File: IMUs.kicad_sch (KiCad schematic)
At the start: 15 parts, among them U501 LSM6DSL, U502 DPS368

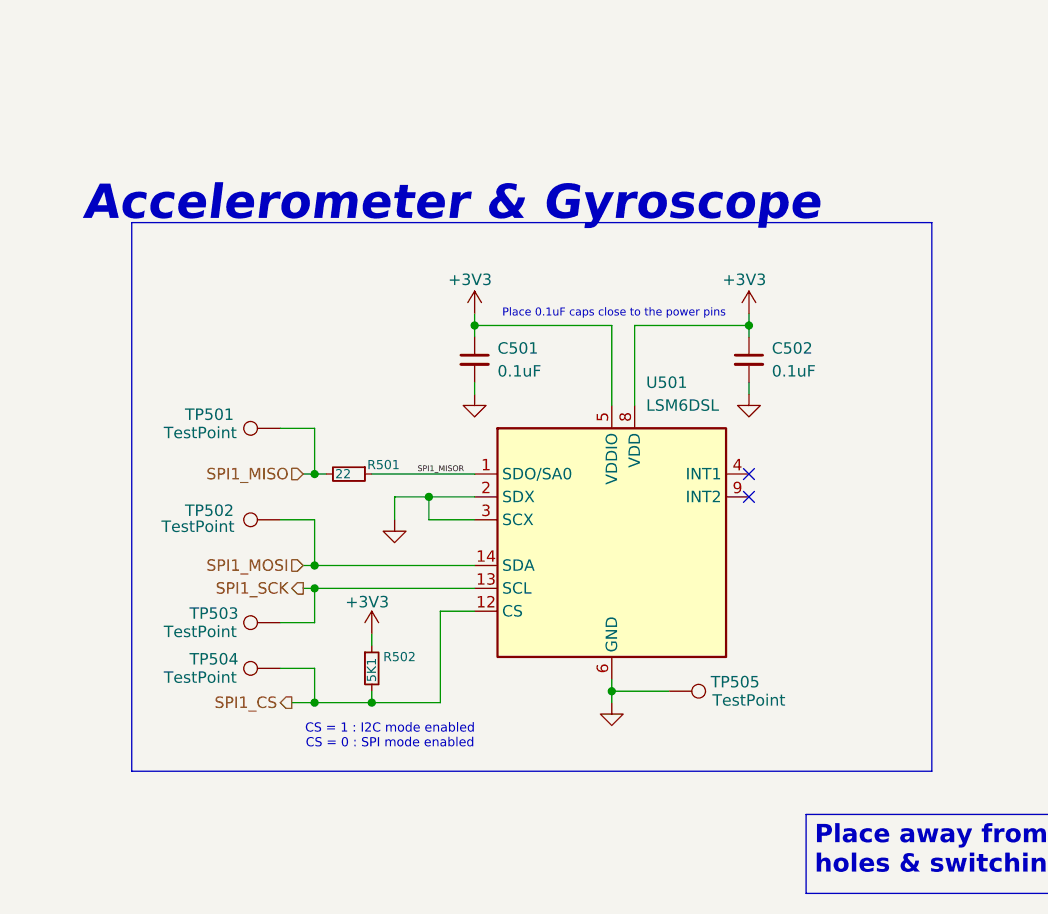
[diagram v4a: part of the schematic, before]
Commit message: refactor: change motor output, renamed power nets
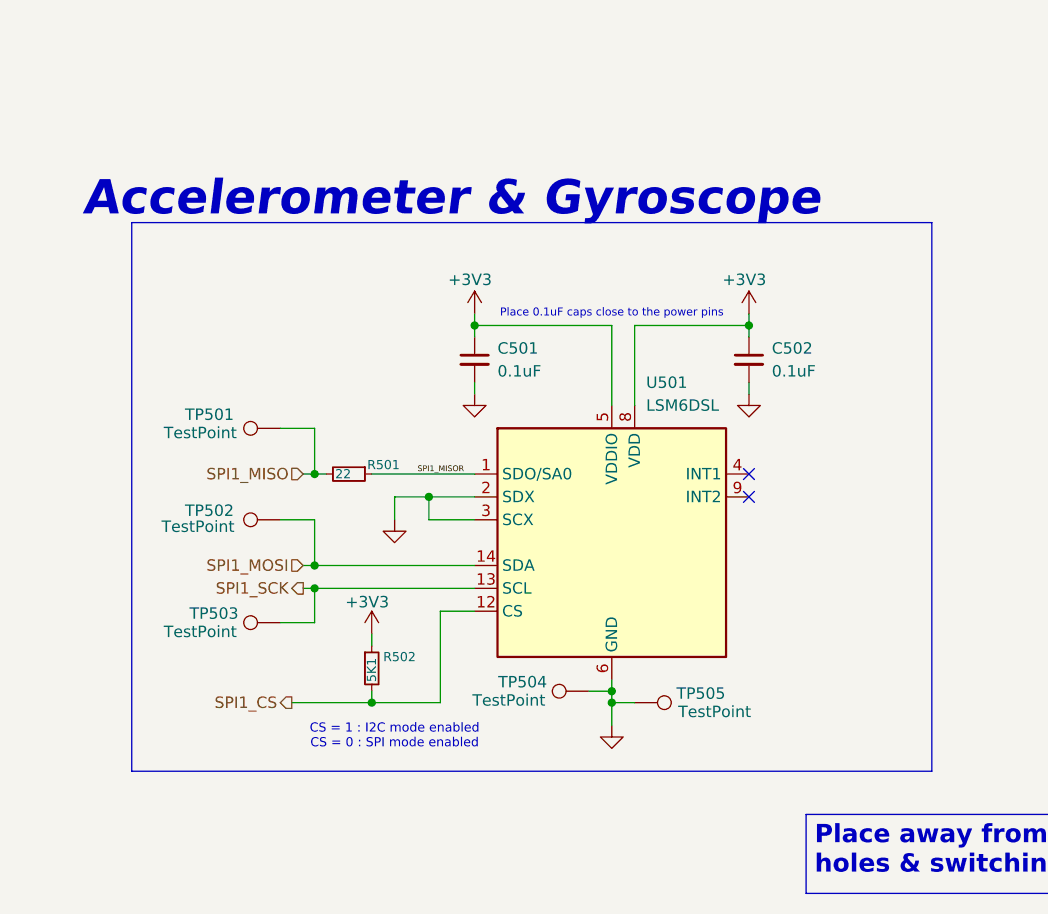
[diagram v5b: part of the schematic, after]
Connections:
- net GND: now also TP504.1
- net SPI1_CS: no longer TP504.1
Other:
- moved on the sheet: TP504, TP505
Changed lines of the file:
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@@
 	(text "Accelerometer & Gyroscope"
 		(exclude_from_sim no)
-		(at 76.2 56.388 0)
+		(at 76.2 55.88 0)
 		(effects
 			(font
@@
 	(text "CS = 1 : I2C mode enabled\nCS = 0 : SPI mode enabled"
 		(exclude_from_sim no)
-		(at 69.342 115.57 0)
+		(at 69.85 115.57 0)
 		(effects
 			(font
@@
 	(text "Place 0.1uF caps close to the power pins"
 		(exclude_from_sim no)
-		(at 94.234 68.58 0)
+		(at 93.98 68.58 0)
 		(effects
 			(font
@@
 	)
 	(junction
-		(at 78.74 69.85)
+		(at 93.98 110.49)
 		(diameter 0)
 		(color 0 0 0 0)
 	)
 	(junction
-		(at 93.98 110.49)
+		(at 78.74 69.85)
 		(diameter 0)
 		(color 0 0 0 0)
@@
 	)
 	(junction
-		(at 219.71 110.49)
+		(at 93.98 111.76)
 		(diameter 0)
 		(color 0 0 0 0)
 	)
 	(junction
-		(at 60.96 111.76)
+		(at 219.71 110.49)
 		(diameter 0)
 		(color 0 0 0 0)
@@
 	(wire
 		(pts
+			(xy 93.98 111.76) (xy 93.98 114.3)
+		)
+		(stroke
+			(width 0)
+			(type default)
+		)
+	)
+	(wire
+		(pts
 			(xy 198.12 80.01) (xy 198.12 77.47)
 		)
@@
 		)
 	)
-	(wire
-		(pts
-			(xy 60.96 107.95) (xy 60.96 111.76)
-		)
-		(stroke
-			(width 0)
-			(type default)
-		)
-	)
 	(polyline
 		(pts
@@
 	(wire
 		(pts
-			(xy 57.15 107.95) (xy 60.96 107.95)
+			(xy 93.98 109.22) (xy 93.98 110.49)
 		)
 		(stroke
@@
 	(wire
 		(pts
-			(xy 60.96 111.76) (xy 67.31 111.76)
+			(xy 58.42 111.76) (xy 67.31 111.76)
 		)
 		(stroke
@@
 	(wire
 		(pts
-			(xy 59.69 96.52) (xy 60.96 96.52)
+			(xy 93.98 110.49) (xy 93.98 111.76)
 		)
 		(stroke
@@
 	(wire
 		(pts
-			(xy 219.71 110.49) (xy 219.71 111.76)
+			(xy 59.69 96.52) (xy 60.96 96.52)
 		)
 		(stroke
@@
 	(wire
 		(pts
-			(xy 67.31 86.36) (xy 78.74 86.36)
+			(xy 219.71 110.49) (xy 219.71 111.76)
 		)
 		(stroke
@@
 	(wire
 		(pts
-			(xy 73.66 88.9) (xy 73.66 91.44)
+			(xy 67.31 86.36) (xy 78.74 86.36)
 		)
 		(stroke
@@
 	(wire
 		(pts
-			(xy 109.22 76.2) (xy 109.22 77.47)
+			(xy 73.66 88.9) (xy 73.66 91.44)
 		)
 		(stroke
@@
 	(wire
 		(pts
-			(xy 100.33 110.49) (xy 93.98 110.49)
+			(xy 109.22 76.2) (xy 109.22 77.47)
 		)
 		(stroke
@@
 	(wire
 		(pts
-			(xy 93.98 109.22) (xy 93.98 110.49)
+			(xy 218.44 107.95) (xy 218.44 110.49)
 		)
 		(stroke
@@
 	(wire
 		(pts
-			(xy 218.44 107.95) (xy 218.44 110.49)
+			(xy 73.66 91.44) (xy 78.74 91.44)
 		)
 		(stroke
@@
 	(wire
 		(pts
-			(xy 73.66 91.44) (xy 78.74 91.44)
+			(xy 91.44 110.49) (xy 93.98 110.49)
 		)
 		(stroke
@@
 	(wire
 		(pts
-			(xy 58.42 111.76) (xy 60.96 111.76)
+			(xy 93.98 111.76) (xy 96.52 111.76)
 		)
 		(stroke
@@
 	(wire
 		(pts
-			(xy 93.98 110.49) (xy 93.98 111.76)
-		)
-		(stroke
-			(width 0)
-			(type default)
-		)
-	)
-	(wire
-		(pts
 			(xy 57.15 102.87) (xy 60.96 102.87)
 		)
@@
 				)
 			)
-			(table_cell "CS1"
+			(table_cell "GND"
 				(exclude_from_sim no)
 				(at 83.82 152.8724 0)
@@
 	(symbol
 		(lib_id "Connector:TestPoint")
-		(at 100.33 110.49 270)
+		(at 96.52 111.76 270)
 		(mirror x)
 		(unit 1)
@@
 		(dnp no)
 		(property "Reference" "TP505"
-			(at 107.696 109.474 90)
+			(at 103.886 110.744 90)
 			(show_name no)
 			(do_not_autoplace no)
@@
 		)
 		(property "Value" "TestPoint"
-			(at 109.22 111.506 90)
+			(at 105.41 112.776 90)
 			(show_name no)
 			(do_not_autoplace no)
@@
 		)
 		(property "Footprint" "TestPoint:TestPoint_Pad_D1.0mm"
-			(at 100.33 105.41 0)
+			(at 96.52 106.68 0)
 			(hide yes)
 			(show_name no)
@@
 		)
 		(property "Datasheet" ""
-			(at 100.33 105.41 0)
+			(at 96.52 106.68 0)
 			(hide yes)
 			(show_name no)
@@
 		)
 		(property "Description" "test point"
-			(at 100.33 110.49 0)
+			(at 96.52 111.76 0)
 			(hide yes)
 			(show_name no)
@@
 		)
 		(property "MANUFACTURER" ""
-			(at 100.33 110.49 90)
+			(at 96.52 111.76 90)
 			(hide yes)
 			(show_name no)
@@
 	(symbol
 		(lib_id "Connector:TestPoint")
-		(at 57.15 107.95 90)
+		(at 91.44 110.49 90)
 		(unit 1)
 		(body_style 1)
@@
 		(dnp no)
 		(property "Reference" "TP504"
-			(at 49.784 106.934 90)
+			(at 84.074 109.474 90)
 			(show_name no)
 			(do_not_autoplace no)
@@
 		)
 		(property "Value" "TestPoint"
-			(at 48.26 108.966 90)
+			(at 82.55 111.506 90)
 			(show_name no)
 			(do_not_autoplace no)
@@
 		)
 		(property "Footprint" "TestPoint:TestPoint_Pad_D1.0mm"
-			(at 57.15 102.87 0)
+			(at 91.44 105.41 0)
 			(hide yes)
 			(show_name no)
@@
 		)
 		(property "Datasheet" ""
-			(at 57.15 102.87 0)
+			(at 91.44 105.41 0)
 			(hide yes)
 			(show_name no)
@@
 		)
 		(property "Description" "test point"
-			(at 57.15 107.95 0)
+			(at 91.44 110.49 0)
 			(hide yes)
 			(show_name no)
@@
 		)
 		(property "MANUFACTURER" ""
-			(at 57.15 107.95 90)
+			(at 91.44 110.49 90)
 			(hide yes)
 			(show_name no)
@@
 	(symbol
 		(lib_id "power:GND")
-		(at 93.98 111.76 0)
+		(at 93.98 114.3 0)
 		(unit 1)
 		(body_style 1)
@@
 		(fields_autoplaced yes)
 		(property "Reference" "#PWR0412"
-			(at 93.98 118.11 0)
+			(at 93.98 120.65 0)
 			(hide yes)
 			(show_name no)
@@
 		)
 		(property "Value" "GND"
-			(at 93.98 116.84 0)
+			(at 93.98 119.38 0)
 			(hide yes)
 			(show_name no)
@@
 		)
 		(property "Footprint" ""
-			(at 93.98 111.76 0)
+			(at 93.98 114.3 0)
 			(hide yes)
 			(show_name no)
@@
 		)
 		(property "Datasheet" ""
-			(at 93.98 111.76 0)
+			(at 93.98 114.3 0)
 			(hide yes)
 			(show_name no)
@@
 		)
 		(property "Description" "Power symbol creates a global label with name \"GND\" , ground"
-			(at 93.98 111.76 0)
+			(at 93.98 114.3 0)
 			(hide yes)
 			(show_name no)
@@
 	(group "LSM6DSL SPI"
 		(lib_id "IMUs:LSM6DSL SPI")
-		(members "0635d062-a8a0-4ab7-88f0-7d733a5d459c" "08d9c76a-1b18-45db-82eb-0e4626e43913"
-			"0b765e13-2ed7-432d-a697-c3ca29f49f38" "0cf15dc8-d53c-4683-8b8e-92e908175e51"
-			"0d03070e-c192-4be7-9a94-1618a9bc21cd" "0d8c7b91-da35-45af-ae05-b3e846dd5df7"
-			"13ae05c6-e3d9-49b6-8595-b7365996df05" "170664c6-93d2-4292-86fc-23b9d99fd96e"
-			"1767fb9c-70b6-4273-bfea-e756556dce41" "20165694-737b-4616-8e9a-13541052ff51"
+		(members "02271870-d62f-482c-9190-c518a8099ff0" "0635d062-a8a0-4ab7-88f0-7d733a5d459c"
+			"08d9c76a-1b18-45db-82eb-0e4626e43913" "0b765e13-2ed7-432d-a697-c3ca29f49f38"
+			"0cf15dc8-d53c-4683-8b8e-92e908175e51" "0d03070e-c192-4be7-9a94-1618a9bc21cd"
+			"0d8c7b91-da35-45af-ae05-b3e846dd5df7" "13ae05c6-e3d9-49b6-8595-b7365996df05"
+			"170664c6-93d2-4292-86fc-23b9d99fd96e" "1767fb9c-70b6-4273-bfea-e756556dce41"
+			"1c69b716-6620-4fe2-bcf3-b7e312a01343" "20165694-737b-4616-8e9a-13541052ff51"
 			"22d103fa-4aea-45ce-b705-d1b4f8811300" "2354545d-b0a0-4344-afad-e2ff9edc77de"
 			"2fe60f43-2c08-4a8c-a8c5-675dd7cd4d70" "38b28923-fb62-4ce0-801f-f4aa6228c4b2"
 			"39754c5f-3e21-4062-ae05-09c1728c5d7e" "412d77bc-9edc-44d0-9f3e-d0b2a599ffdd"
-			"50bc12aa-8f9a-4f9b-b2d9-7299a935ae70" "50febd7a-352d-4c65-b0cb-518139e5077c"
-			"52ace526-fbef-42ef-8ec4-49042cb38c17" "5469c8d6-7cbd-49e1-922e-f0e568591383"
-			"57602b03-536e-438a-85dc-25fd0f903f01" "62a35531-832c-452e-8d9f-0abf028220ed"
-			"6330f4bf-415e-4753-b8c6-d06f67f62c48" "665a796b-1f5c-4f64-820e-6bf27b1fe02f"
+			"4d0f1608-37d5-48fb-9881-102292186f8d" "50bc12aa-8f9a-4f9b-b2d9-7299a935ae70"
+			"50febd7a-352d-4c65-b0cb-518139e5077c" "52ace526-fbef-42ef-8ec4-49042cb38c17"
+			"5469c8d6-7cbd-49e1-922e-f0e568591383" "57602b03-536e-438a-85dc-25fd0f903f01"
+			"62a35531-832c-452e-8d9f-0abf028220ed" "6330f4bf-415e-4753-b8c6-d06f67f62c48"
+			"665a796b-1f5c-4f64-820e-6bf27b1fe02f" "669c7fd5-ec94-4187-9cf5-444391b4eca9"
 			"66dc0654-e60c-4bbe-8403-11d5cb7237f0" "71b85ac5-3ed6-4770-8e4a-75bc843da810"
 			"74b72755-23ff-4ccb-bf83-0421d1ba93d5" "76940594-1dae-4213-9b2b-bcc8dd82604b"
 			"7ef96c2e-f66f-40c5-9102-15e50c709d6c" "7f7d6229-e001-4ffe-9c2a-76c6d6886585"
-			"816d7a37-0b5e-4fdb-a295-fd8b0feeccf4" "85138827-62de-4748-94c0-5f3ecb8193d5"
-			"87120c0a-b8b2-43d4-acd1-1990f6fc0408" "88cee71e-28d2-4dbd-86ec-334a81b75eb3"
-			"8aa3f7a8-de52-4b5d-817a-219ec4198cb3" "8d18a69e-c242-4cf8-9f27-90c527ac26ff"
-			"8e558f2e-83f1-457f-bc6b-007efdd70686" "8f79b2a3-c12a-4c2c-b5b2-9b13de51af1d"
-			"94a9712d-524d-4a05-b78c-01201ec4167c" "a0004538-6282-42c8-b5e6-1e07503390af"
-			"aea3631f-6b1d-4c32-b3cc-d2c94224a198" "b03277cb-607d-4945-9fbd-b7127e486f3b"
-			"b27772a1-4e6b-4400-932f-c07c3d349c19" "b590be60-7cb4-4cb8-9bb7-4a80ec985545"
-			"c0cae175-4040-4baa-a449-0e1fb7770943" "d07657d3-82a4-434b-8cd6-003562c17a04"
-			"d0b0d9e1-6eda-4c21-9ba4-a6982ab1a460" "d2ced081-06a8-4a65-bad1-d48ec5a7a521"
+			"816d7a37-0b5e-4fdb-a295-fd8b0feeccf4" "82d1c826-a63f-4664-8f65-dc05eb82c265"
+			"85138827-62de-4748-94c0-5f3ecb8193d5" "87120c0a-b8b2-43d4-acd1-1990f6fc0408"
+			"88cee71e-28d2-4dbd-86ec-334a81b75eb3" "8aa3f7a8-de52-4b5d-817a-219ec4198cb3"
+			"8d18a69e-c242-4cf8-9f27-90c527ac26ff" "8e558f2e-83f1-457f-bc6b-007efdd70686"
+			"8f79b2a3-c12a-4c2c-b5b2-9b13de51af1d" "94a9712d-524d-4a05-b78c-01201ec4167c"
+			"a0004538-6282-42c8-b5e6-1e07503390af" "aea3631f-6b1d-4c32-b3cc-d2c94224a198"
+			"b03277cb-607d-4945-9fbd-b7127e486f3b" "b27772a1-4e6b-4400-932f-c07c3d349c19"
+			"b590be60-7cb4-4cb8-9bb7-4a80ec985545" "c0cae175-4040-4baa-a449-0e1fb7770943"
+			"d07657d3-82a4-434b-8cd6-003562c17a04" "d0b0d9e1-6eda-4c21-9ba4-a6982ab1a460"
 			"d4ae8920-0eb7-40fa-a104-215bc1ba82a7" "d5e7bc8b-1bed-4650-9ab9-2f97601ae224"
-			"d621e954-2bef-46f6-a896-69206058b090" "dc75e533-7be1-41b6-a29c-ae15edcd1e46"
-			"e804b3be-158c-4b5a-93ae-a4c0e2602026" "ea39a907-af77-45fe-a483-6424465d1ac2"
-			"eb9c6634-1dce-47c8-b744-7efd756a19fd" "ee743029-0630-4fdc-b3c5-bf50ecad0b3c"
+			"d621e954-2bef-46f6-a896-69206058b090" "d738dba5-7f63-429a-bb23-8feeaa84baee"
+			"e25bb97f-cc69-466d-9486-5c6e71f66ac1" "e804b3be-158c-4b5a-93ae-a4c0e2602026"
+			"ea39a907-af77-45fe-a483-6424465d1ac2" "eb9c6634-1dce-47c8-b744-7efd756a19fd"
+			"ee743029-0630-4fdc-b3c5-bf50ecad0b3c"
 		)
 	)
